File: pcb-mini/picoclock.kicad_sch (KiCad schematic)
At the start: 64 parts, among them J1 UART, J10 USB, J11 Alt Power, J12 LED_5V, J2 USB_A, J4 xx, J5 Micro_SD_Card_Det1, J6 USB_C_Receptacle, J9 AUDIO, Q1 BSS138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

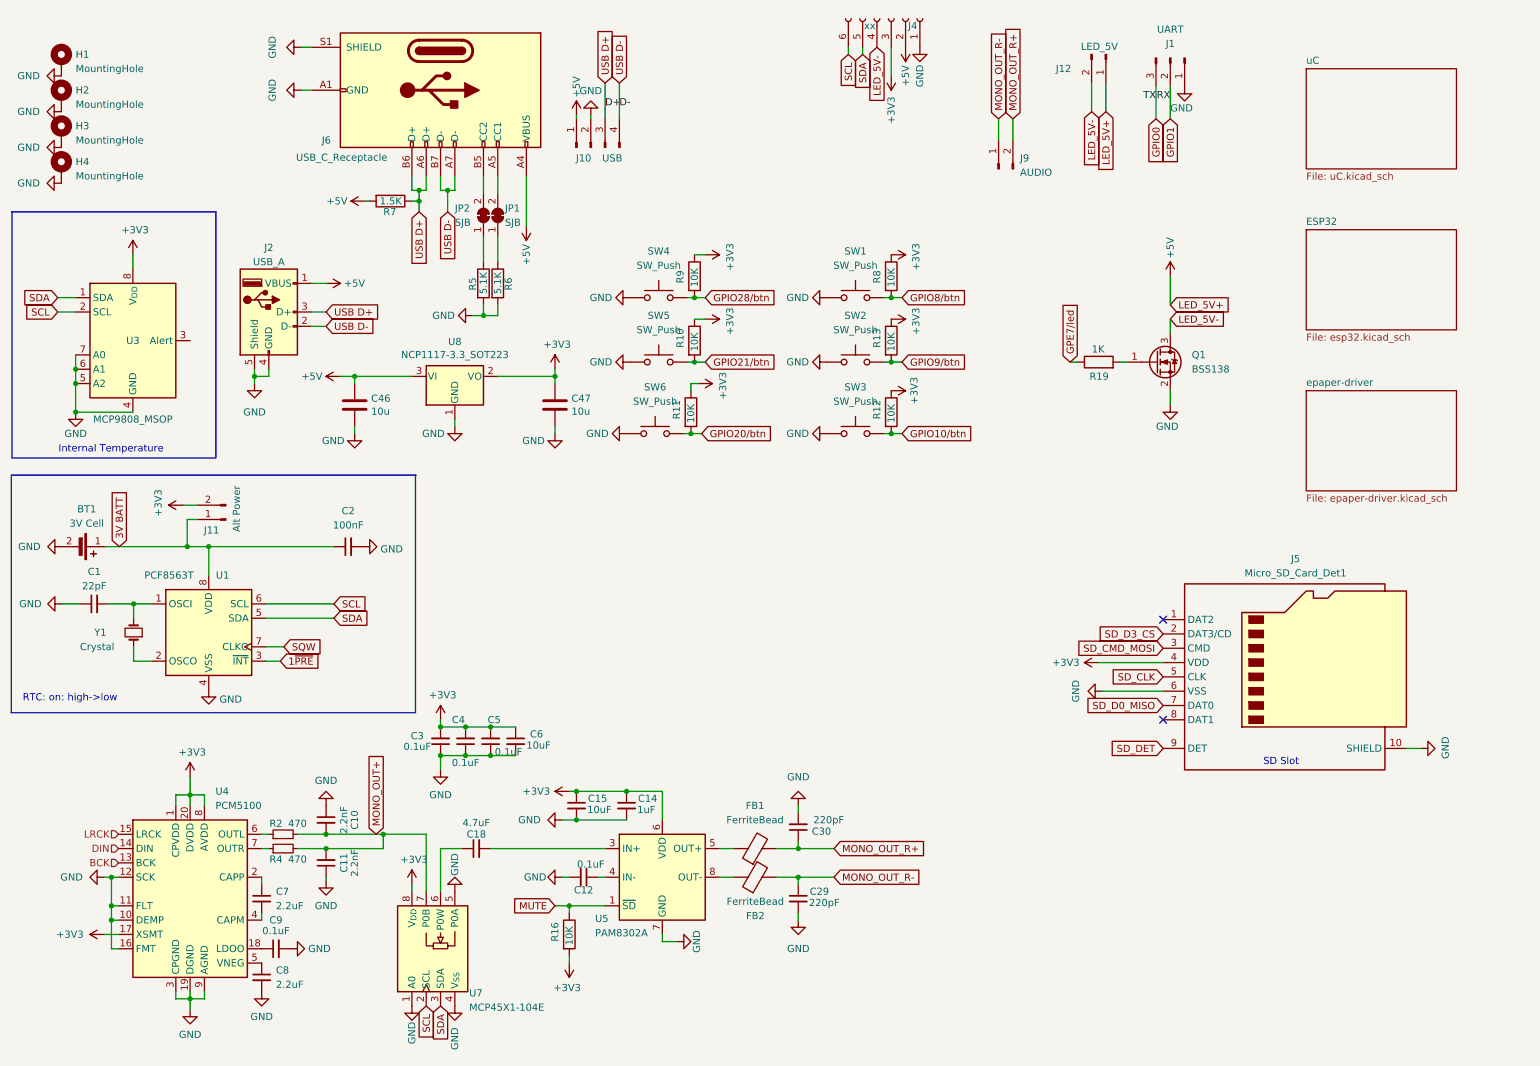
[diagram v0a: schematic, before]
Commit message: [pcb-mini] add ESP32, RM2, route most things
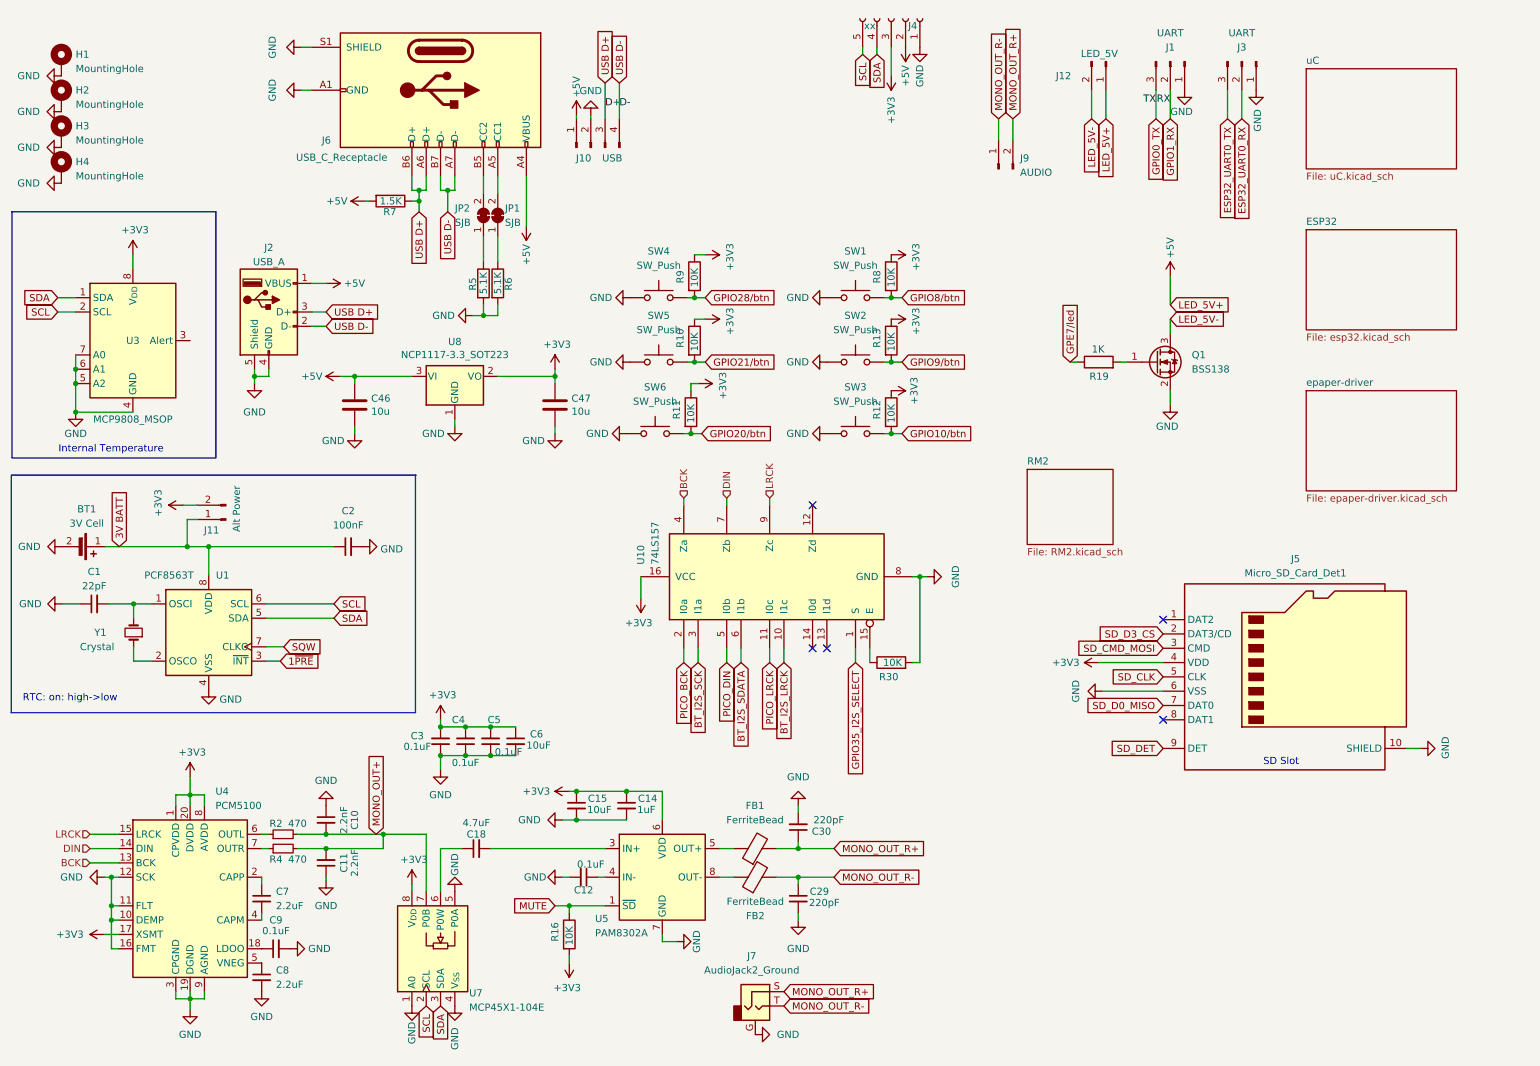
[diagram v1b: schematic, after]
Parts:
- added J3: UART, Connector_PinHeader_2.54mm:PinHeader_1x03_P2.54mm_Vertical, symbol Connector:Conn_01x03_Pin
- added J7: AudioJack2_Ground, Connector_Audio:Jack_3.5mm_QingPu_WQP-PJ398SM_Vertical_CircularHoles, symbol Connector_Audio:AudioJack2_Ground
- added R30: 10K, Resistor_SMD:R_0603_1608Metric, symbol Device:R
- added U10: 74LS157, Package_SO:TSSOP-16_4.4x5mm_P0.65mm, symbol 74xx:74LS157
- J4: footprint Connector_PinSocket_2.54mm:PinSocket_1x06_P2.54mm_Vertical -> Connector_PinSocket_2.54mm:PinSocket_1x05_P2.54mm_Vertical; symbol Connector:Conn_01x06_Socket -> Connector:Conn_01x05_Socket
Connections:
- net +3V3: now also U10.16 (VCC)
- net BCK: now also U10.4 (Za)
- net DIN: now also U10.7 (Zb)
- net GND: now also J3.1 (Pin_1), J7.G, R30.2, U10.8 (GND)
- net LED_5V-: no longer J4.4 (Pin_4)
- net LRCK: now also U10.9 (Zc)
- net MONO_OUT_R+: now also J7.S
- net MONO_OUT_R-: now also J7.T
- net SCL: now also J4.5 (Pin_5); no longer J4.6 (Pin_6)
- net SDA: now also J4.4 (Pin_4); no longer J4.5 (Pin_5)
- net GPIO0 renamed GPIO0_TX
- net GPIO1 renamed GPIO1_RX
- new net: R30.1, U10.15 (E)
- new net BT_I2S_LRCK: U10.10 (I1c)
- new net BT_I2S_SCK: U10.3 (I1a)
- new net BT_I2S_SDATA: U10.6 (I1b)
- new net ESP32_UART0_RX: J3.2 (Pin_2)
- new net ESP32_UART0_TX: J3.3 (Pin_3)
- new net GPIO35_I2S_SELECT: U10.1 (S)
- new net PICO_BCK: U10.2 (I0a)
- new net PICO_DIN: U10.5 (I0b)
- new net PICO_LRCK: U10.11 (I0c)
- no-connect marks 2 -> 5
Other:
- added sheet RM2 (RM2.kicad_sch)
- moved on the sheet: J1, J12

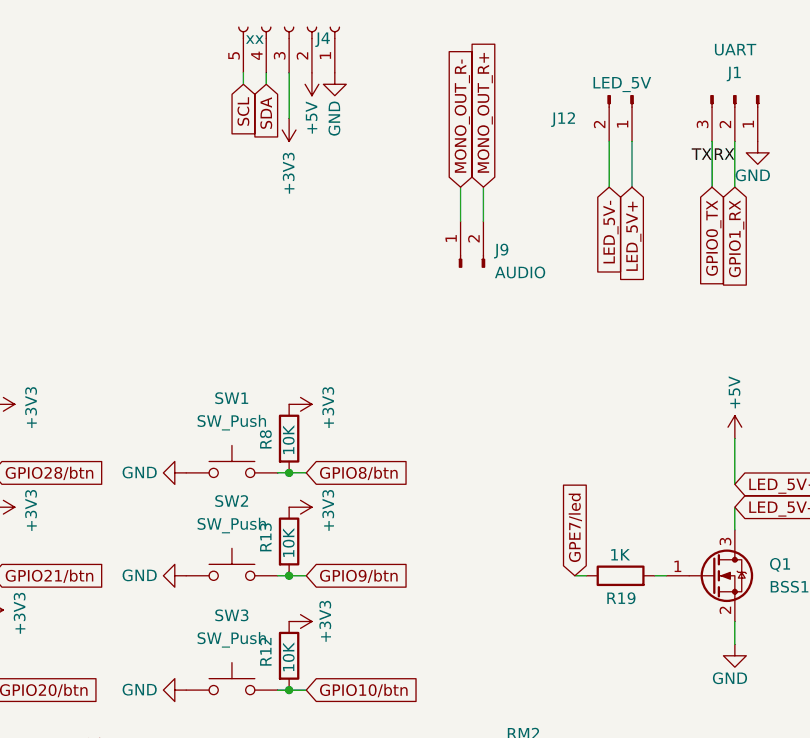
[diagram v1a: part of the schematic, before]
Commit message: [pcb-mini] fix warnings/errors
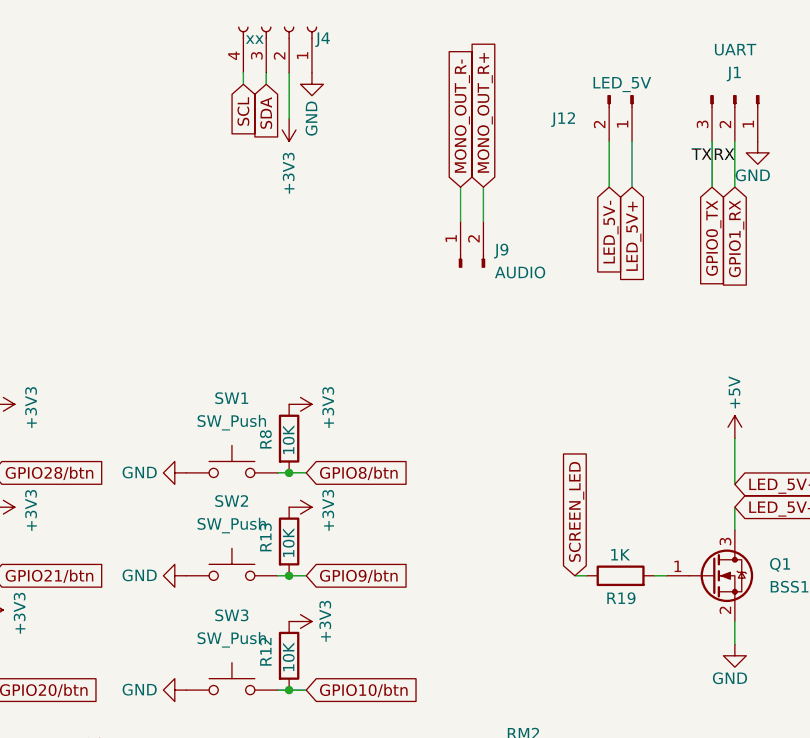
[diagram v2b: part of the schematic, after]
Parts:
- J4: footprint Connector_PinSocket_2.54mm:PinSocket_1x05_P2.54mm_Vertical -> Connector_PinSocket_2.54mm:PinSocket_1x04_P2.54mm_Vertical; symbol Connector:Conn_01x05_Socket -> Connector:Conn_01x04_Socket
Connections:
- net +3V3: now also J4.2 (Pin_2); no longer J4.3 (Pin_3)
- net +5V: no longer J4.2 (Pin_2)
- net SCL: now also J4.4 (Pin_4); no longer J4.5 (Pin_5)
- net SDA: now also J4.3 (Pin_3); no longer J4.4 (Pin_4)
- net GPE7/led renamed SCREEN_LED
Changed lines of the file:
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@@
 		)
 	)
+	(wire
+		(pts
+			(xy 167.64 20.32) (xy 167.64 19.05)
+		)
+		(stroke
+			(width 0)
+			(type default)
+		)
+	)
 	(polyline
 		(pts
@@
 	(wire
 		(pts
+			(xy 170.18 24.13) (xy 170.18 19.05)
+		)
+		(stroke
+			(width 0)
+			(type default)
+		)
+	)
+	(wire
+		(pts
 			(xy 30.48 176.53) (xy 33.02 176.53)
 		)
@@
 	(wire
 		(pts
-			(xy 165.1 20.32) (xy 165.1 19.05)
-		)
-		(stroke
-			(width 0)
-			(type default)
-		)
-	)
-	(wire
-		(pts
 			(xy 86.36 46.355) (xy 86.36 44.45)
 		)
@@
 	(wire
 		(pts
-			(xy 170.18 24.13) (xy 170.18 19.05)
-		)
-		(stroke
-			(width 0)
-			(type default)
-		)
-	)
-	(wire
-		(pts
 			(xy 153.67 173.99) (xy 153.67 172.72)
 		)
@@
 	(wire
 		(pts
-			(xy 167.64 20.32) (xy 167.64 19.05)
-		)
-		(stroke
-			(width 0)
-			(type default)
-		)
-	)
-	(wire
-		(pts
 			(xy 85.09 167.64) (xy 85.09 168.91)
 		)
@@
 	(wire
 		(pts
+			(xy 165.1 20.32) (xy 165.1 19.05)
+		)
+		(stroke
+			(width 0)
+			(type default)
+		)
+	)
+	(wire
+		(pts
 			(xy 87.63 158.75) (xy 87.63 168.91)
 		)
@@
 		)
 	)
-	(global_label "SCL"
-		(shape input)
-		(at 165.1 20.32 270)
-		(fields_autoplaced yes)
-		(effects
-			(font
-				(size 1.27 1.27)
-			)
-			(justify right)
-		)
-		(property "Intersheetrefs" "${INTERSHEET_REFS}"
-			(at 165.1 26.8128 90)
-			(effects
-				(font
-					(size 1.27 1.27)
-				)
-				(justify right)
-				(hide yes)
-			)
-		)
-	)
 	(global_label "USB D+"
 		(shape input)
@@
 		)
 	)
-	(global_label "GPE7{slash}led"
+	(global_label "SCREEN_LED"
 		(shape input)
 		(at 201.93 74.93 90)
@@
 		)
 		(property "Intersheetrefs" "${INTERSHEET_REFS}"
-			(at 201.93 62.813 90)
+			(at 201.93 60.1521 90)
 			(effects
 				(font
@@
 		)
 	)
+	(global_label "SDA"
+		(shape input)
+		(at 167.64 20.32 270)
+		(fields_autoplaced yes)
+		(effects
+			(font
+				(size 1.27 1.27)
+			)
+			(justify right)
+		)
+		(property "Intersheetrefs" "${INTERSHEET_REFS}"
+			(at 167.64 26.8733 90)
+			(effects
+				(font
+					(size 1.27 1.27)
+				)
+				(justify right)
+				(hide yes)
+			)
+		)
+	)
 	(global_label "MONO_OUT_R-"
 		(shape input)
@@
 		)
 	)
+	(global_label "SCL"
+		(shape input)
+		(at 165.1 20.32 270)
+		(fields_autoplaced yes)
+		(effects
+			(font
+				(size 1.27 1.27)
+			)
+			(justify right)
+		)
+		(property "Intersheetrefs" "${INTERSHEET_REFS}"
+			(at 165.1 26.8128 90)
+			(effects
+				(font
+					(size 1.27 1.27)
+				)
+				(justify right)
+				(hide yes)
+			)
+		)
+	)
 	(global_label "GPIO9{slash}btn"
 		(shape input)
@@
 		)
 	)
-	(global_label "SDA"
-		(shape input)
-		(at 167.64 20.32 270)
-		(fields_autoplaced yes)
-		(effects
-			(font
-				(size 1.27 1.27)
-			)
-			(justify right)
-		)
-		(property "Intersheetrefs" "${INTERSHEET_REFS}"
-			(at 167.64 26.8733 90)
-			(effects
-				(font
-					(size 1.27 1.27)
-				)
-				(justify right)
-				(hide yes)
-			)
-		)
-	)
 	(global_label "BT_I2S_SDATA"
 		(shape input)
@@
 	(symbol
 		(lib_id "power:GND")
-		(at 175.26 19.05 0)
+		(at 172.72 19.05 0)
 		(unit 1)
 		(exclude_from_sim no)
@@
 		(dnp no)
 		(property "Reference" "#PWR022"
-			(at 175.26 25.4 0)
+			(at 172.72 25.4 0)
 			(effects
 				(font
@@
 		)
 		(property "Value" "GND"
-			(at 175.26 24.13 90)
+			(at 172.72 24.13 90)
 			(effects
 				(font
@@
 		)
 		(property "Footprint" ""
-			(at 175.26 19.05 0)
+			(at 172.72 19.05 0)
 			(effects
 				(font
@@
 		)
 		(property "Datasheet" ""
-			(at 175.26 19.05 0)
+			(at 172.72 19.05 0)
 			(effects
 				(font
@@
 		)
 		(property "Description" ""
-			(at 175.26 19.05 0)
+			(at 172.72 19.05 0)
 			(effects
 				(font
@@
 	)
 	(symbol
-		(lib_id "power:+5V")
-		(at 172.72 19.05 180)
-		(unit 1)
-		(exclude_from_sim no)
-		(in_bom yes)
-		(on_board yes)
-		(dnp no)
-		(property "Reference" "#PWR070"
-			(at 172.72 15.24 0)
-			(effects
-				(font
-					(size 1.27 1.27)
-				)
-				(hide yes)
-			)
-		)
-		(property "Value" "+5V"
-			(at 172.72 22.225 90)
-			(effects
-				(font
-					(size 1.27 1.27)
-				)
-				(justify left)
-			)
-		)
-		(property "Footprint" ""
-			(at 172.72 19.05 0)
-			(effects
-				(font
-					(size 1.27 1.27)
-				)
-				(hide yes)
-			)
-		)
-		(property "Datasheet" ""
-			(at 172.72 19.05 0)
-			(effects
-				(font
-					(size 1.27 1.27)
-				)
-				(hide yes)
-			)
-		)
-		(property "Description" ""
-			(at 172.72 19.05 0)
-			(effects
-				(font
-					(size 1.27 1.27)
-				)
-				(hide yes)
-			)
-		)
-		(pin "1"
-		)
-		(instances
-			(project "picoclock"
-				(path "/3b9dec0e-e0b7-4565-afc9-c4692f41aea9"
-					(reference "#PWR070")
-					(unit 1)
-				)
-			)
-		)
-	)
-	(symbol
 		(lib_id "Switch:SW_Push")
 		(at 128.905 63.5 0)
@@
 	)
 	(symbol
-		(lib_id "Connector:Conn_01x05_Socket")
+		(lib_id "Connector:Conn_01x04_Socket")
 		(at 170.18 13.97 270)
 		(mirror x)
@@
 			)
 		)
-		(property "Footprint" "Connector_PinSocket_2.54mm:PinSocket_1x05_P2.54mm_Vertical"
+		(property "Footprint" "Connector_PinSocket_2.54mm:PinSocket_1x04_P2.54mm_Vertical"
 			(at 170.18 13.97 0)
 			(effects
@@
 			)
 		)
-		(property "Description" "Generic connector, single row, 01x05, script generated"
+		(property "Description" "Generic connector, single row, 01x04, script generated"
 			(at 170.18 13.97 0)
 			(effects
@@
 		(pin "4"
 		)
-		(pin "5"
-		)
 		(instances
